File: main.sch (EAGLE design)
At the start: 27 parts, among them IC1 FT232RL, U1 ATMEGA328P_TQFP, Y3 16MHz

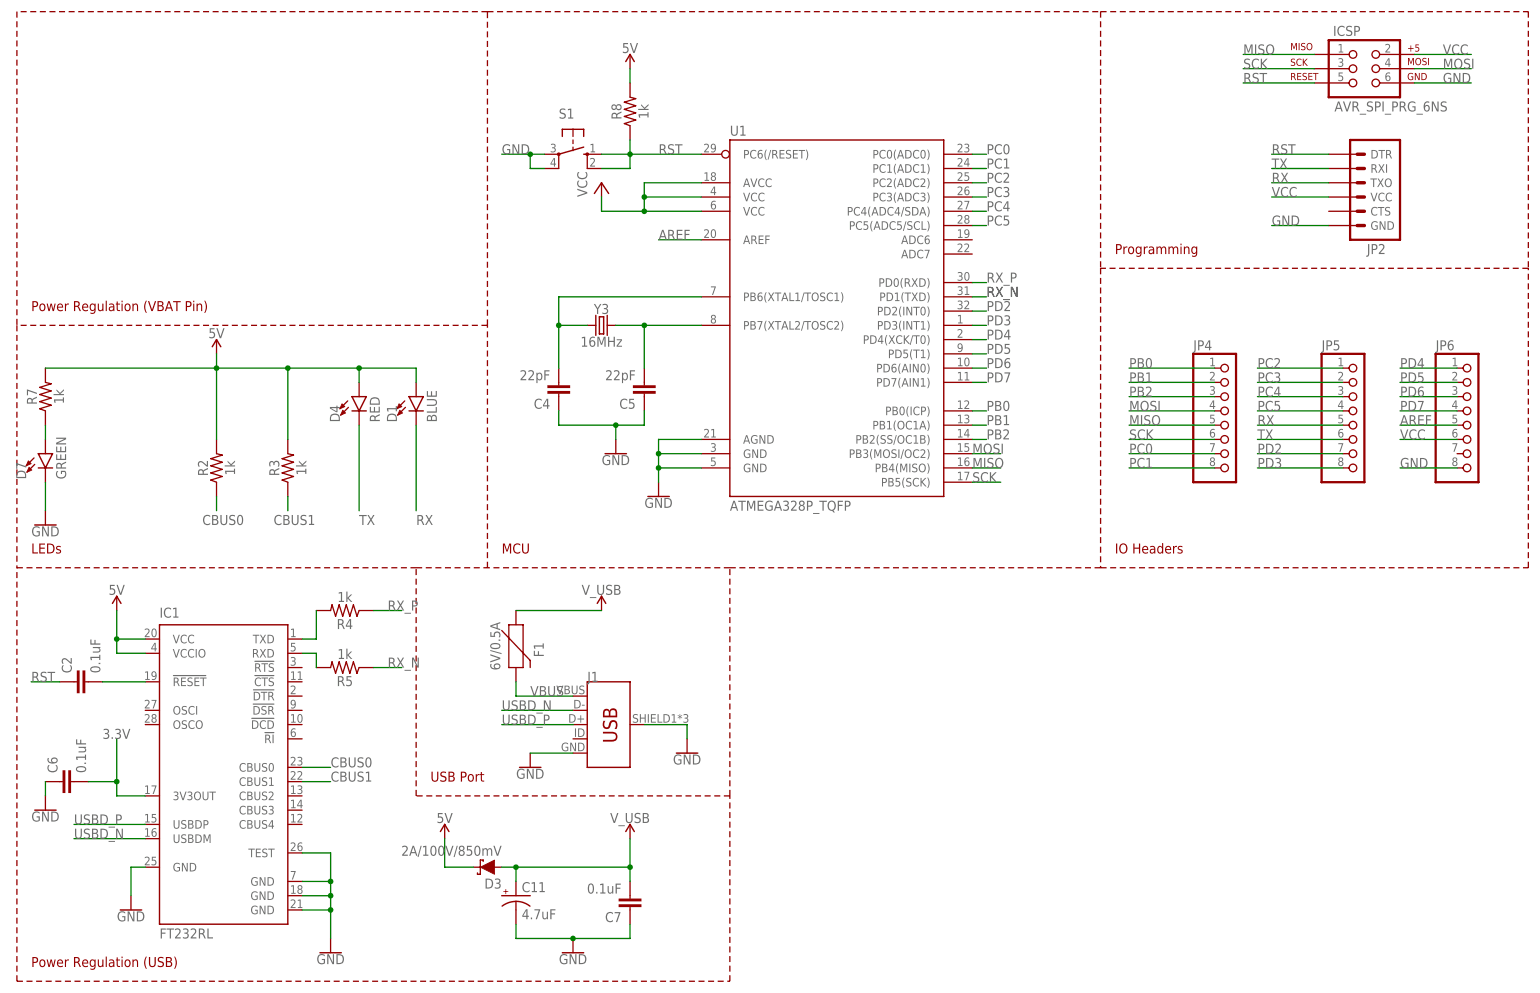
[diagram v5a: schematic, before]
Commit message: Fixed DRC Errors
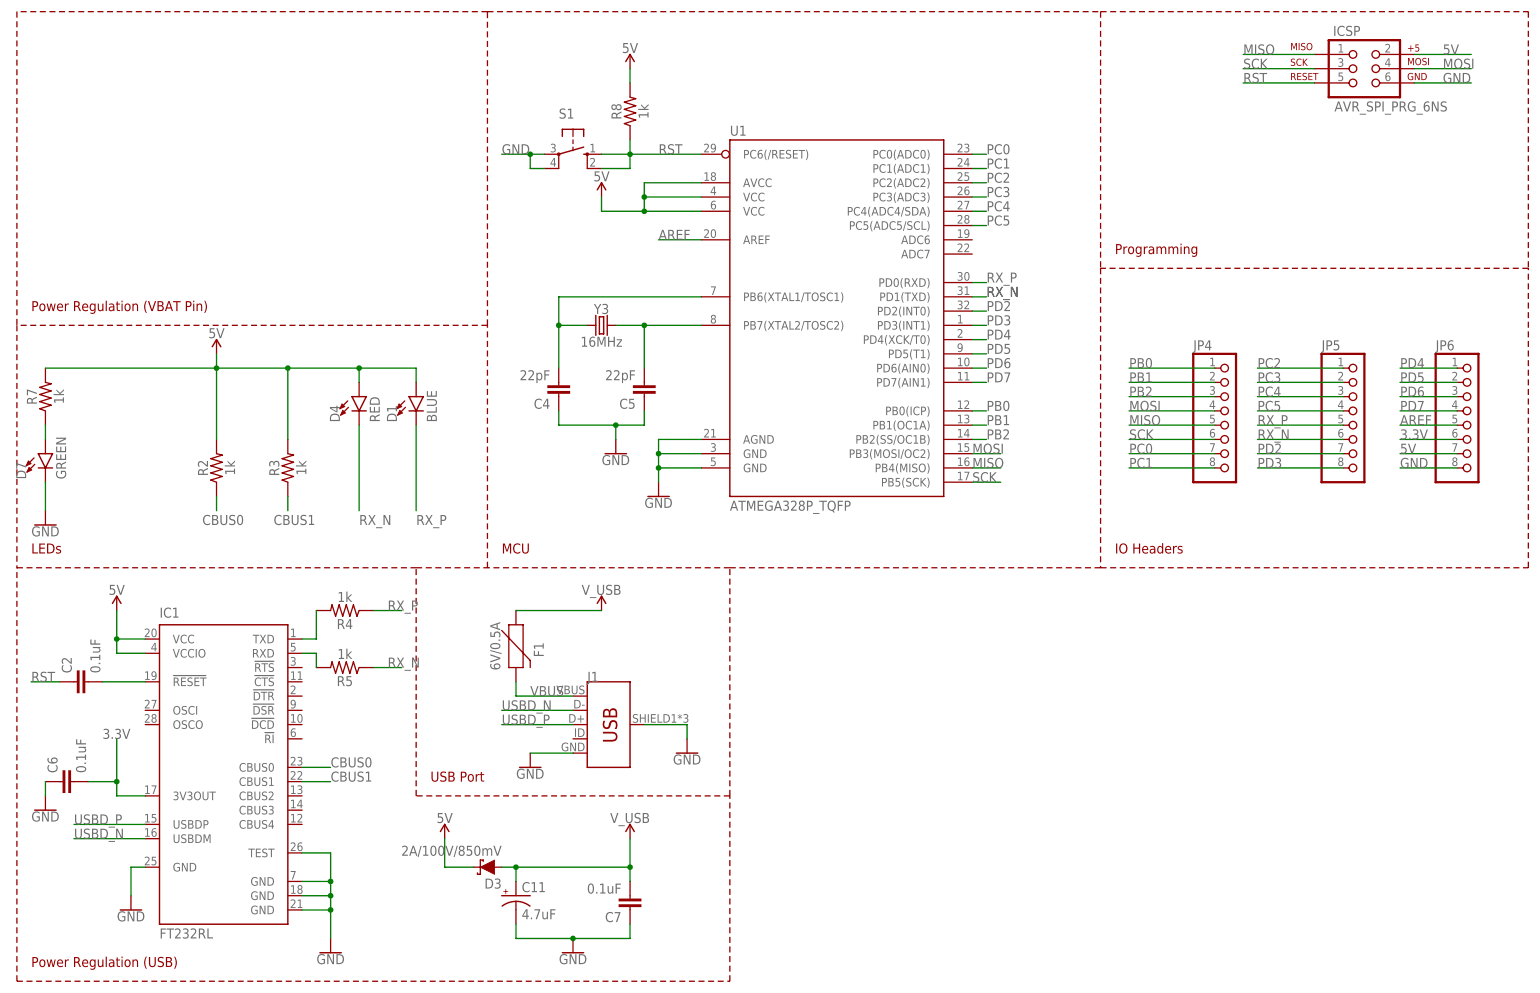
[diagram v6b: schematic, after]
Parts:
- removed JP2: (no value), SparkFun-Connectors:ARDUINO_SERIAL_PROGRAMLOCK
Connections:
- removed net RX: D1.C, JP2.TXO, JP5.5
- removed net TX: D4.C, JP2.RXI, JP5.6
- removed net VCC: ICSP.2, JP2.VCC, JP6.6, U1.AVCC, U1.VCC@4, U1.VCC@6
- net 3.3V: now also JP6.6
- net 5V: now also ICSP.2, JP6.7, U1.AVCC, U1.VCC@4, U1.VCC@6
- net GND: no longer JP2.GND
- net RST: no longer JP2.DTR
- net RX_N: now also D4.C, JP5.6
- net RX_P: now also D1.C, JP5.5
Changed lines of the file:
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@@
 <parts>
 <part name="ICSP" library="SparkFun-Connectors" deviceset="AVR_SPI_PRG_6" device="NS"/>
-<part name="JP2" library="SparkFun-Connectors" deviceset="ARDUINO_SERIAL_PROGRAM" device="LOCK"/>
 <part name="JP4" library="pinhead" library_urn="urn:adsk.eagle:library:325" deviceset="PINHD-1X8" device=""/>
 <part name="JP5" library="pinhead" library_urn="urn:adsk.eagle:library:325" deviceset="PINHD-1X8" device=""/>
@@
 <part name="D1" library="SparkFun-LED" deviceset="LED-BLUE" device="0603" value="BLUE"/>
 <part name="IC1" library="ftdichip" library_urn="urn:adsk.eagle:library:231" deviceset="FT232R" device="L"/>
-<part name="P+4" library="supply1" library_urn="urn:adsk.eagle:library:371" deviceset="VCC" device=""/>
 <part name="J1" library="SparkFun-Connectors" deviceset="USB_MICRO-B" device="_FEMALE-SMT"/>
 <part name="F1" library="SparkFun-Fuses" deviceset="PPTC" device="_HALF-AMP" value="6V/0.5A"/>
@@
 <part name="D7" library="SparkFun-LED" deviceset="LED-GREEN" device="0603" value="GREEN"/>
 <part name="D4" library="SparkFun-LED" deviceset="LED-RED" device="0603" value="RED"/>
+<part name="SUPPLY3" library="SparkFun-PowerSymbols" deviceset="5V" device=""/>
 </parts>
 <sheets>
@@
 <instances>
 <instance part="ICSP" gate="G$1" x="198.12" y="144.78"/>
-<instance part="JP2" gate="G$1" x="198.12" y="124.46" rot="R180"/>
 <instance part="JP4" gate="A" x="175.26" y="81.28"/>
 <instance part="JP5" gate="A" x="198.12" y="81.28"/>
@@
 <instance part="D1" gate="G$1" x="30.48" y="86.36"/>
 <instance part="IC1" gate="1" x="-5.08" y="20.32"/>
-<instance part="P+4" gate="VCC" x="63.5" y="124.46"/>
 <instance part="J1" gate="G$1" x="63.5" y="27.94"/>
 <instance part="F1" gate="G$1" x="48.26" y="43.18" rot="R270"/>
@@
 <instance part="D7" gate="G$1" x="-35.56" y="76.2"/>
 <instance part="D4" gate="G$1" x="20.32" y="86.36"/>
+<instance part="SUPPLY3" gate="G$1" x="63.5" y="121.92"/>
 </instances>
 <busses>
@@
 <wire x1="208.28" y1="142.24" x2="218.44" y2="142.24" width="0.1524" layer="91"/>
 <label x="213.36" y="142.24" size="1.778" layer="95"/>
-</segment>
-<segment>
-<pinref part="JP2" gate="G$1" pin="GND"/>
-<wire x1="193.04" y1="116.84" x2="182.88" y2="116.84" width="0.1524" layer="91"/>
-<label x="182.88" y="116.84" size="1.778" layer="95"/>
 </segment>
 <segment>
@@
 </segment>
 </net>
-<net name="VCC" class="3">
-<segment>
-<pinref part="ICSP" gate="G$1" pin="2"/>
-<wire x1="208.28" y1="147.32" x2="218.44" y2="147.32" width="0.1524" layer="91"/>
-<label x="213.36" y="147.32" size="1.778" layer="95"/>
-</segment>
-<segment>
-<pinref part="JP2" gate="G$1" pin="VCC"/>
-<wire x1="193.04" y1="121.92" x2="182.88" y2="121.92" width="0.1524" layer="91"/>
-<label x="182.88" y="121.92" size="1.778" layer="95"/>
-</segment>
-<segment>
-<pinref part="JP6" gate="A" pin="6"/>
-<wire x1="215.9" y1="78.74" x2="205.74" y2="78.74" width="0.1524" layer="91"/>
-<label x="205.74" y="78.74" size="1.778" layer="95"/>
-</segment>
-<segment>
-<wire x1="81.28" y1="121.92" x2="71.12" y2="121.92" width="0.1524" layer="91"/>
-<wire x1="81.28" y1="124.46" x2="71.12" y2="124.46" width="0.1524" layer="91"/>
-<wire x1="81.28" y1="119.38" x2="71.12" y2="119.38" width="0.1524" layer="91"/>
-<wire x1="71.12" y1="119.38" x2="71.12" y2="121.92" width="0.1524" layer="91"/>
-<wire x1="71.12" y1="121.92" x2="71.12" y2="124.46" width="0.1524" layer="91"/>
-<junction x="71.12" y="121.92"/>
-<wire x1="71.12" y1="119.38" x2="63.5" y2="119.38" width="0.1524" layer="91"/>
-<junction x="71.12" y="119.38"/>
-<pinref part="P+4" gate="VCC" pin="VCC"/>
-<wire x1="63.5" y1="119.38" x2="63.5" y2="121.92" width="0.1524" layer="91"/>
-<pinref part="U1" gate="U$1" pin="VCC@4"/>
-<pinref part="U1" gate="U$1" pin="VCC@6"/>
-<pinref part="U1" gate="U$1" pin="AVCC"/>
-</segment>
-</net>
 <net name="RST" class="0">
 <segment>
@@
 </segment>
 <segment>
-<wire x1="193.04" y1="129.54" x2="182.88" y2="129.54" width="0.1524" layer="91"/>
-<label x="182.88" y="129.54" size="1.778" layer="95"/>
-<pinref part="JP2" gate="G$1" pin="DTR"/>
-</segment>
-<segment>
 <wire x1="-33.02" y1="35.56" x2="-38.1" y2="35.56" width="0.1524" layer="91"/>
 <label x="-38.1" y="35.56" size="1.778" layer="95"/>
@@
 <wire x1="172.72" y1="83.82" x2="157.48" y2="83.82" width="0.1524" layer="91"/>
 <label x="157.48" y="83.82" size="1.778" layer="95"/>
-</segment>
-</net>
-<net name="TX" class="0">
-<segment>
-<pinref part="JP2" gate="G$1" pin="RXI"/>
-<wire x1="193.04" y1="127" x2="182.88" y2="127" width="0.1524" layer="91"/>
-<label x="182.88" y="127" size="1.778" layer="95"/>
-</segment>
-<segment>
-<pinref part="JP5" gate="A" pin="6"/>
-<wire x1="195.58" y1="78.74" x2="180.34" y2="78.74" width="0.1524" layer="91"/>
-<label x="180.34" y="78.74" size="1.778" layer="95"/>
-</segment>
-<segment>
-<label x="20.32" y="63.5" size="1.778" layer="95"/>
-<pinref part="D4" gate="G$1" pin="C"/>
-<wire x1="20.32" y1="66.04" x2="20.32" y2="81.28" width="0.1524" layer="91"/>
-</segment>
-</net>
-<net name="RX" class="0">
-<segment>
-<pinref part="JP2" gate="G$1" pin="TXO"/>
-<wire x1="193.04" y1="124.46" x2="182.88" y2="124.46" width="0.1524" layer="91"/>
-<label x="182.88" y="124.46" size="1.778" layer="95"/>
-</segment>
-<segment>
-<pinref part="JP5" gate="A" pin="5"/>
-<wire x1="195.58" y1="81.28" x2="180.34" y2="81.28" width="0.1524" layer="91"/>
-<label x="180.34" y="81.28" size="1.778" layer="95"/>
-</segment>
-<segment>
-<label x="30.48" y="63.5" size="1.778" layer="95"/>
-<pinref part="D1" gate="G$1" pin="C"/>
-<wire x1="30.48" y1="66.04" x2="30.48" y2="81.28" width="0.1524" layer="91"/>
 </segment>
 </net>
@@
 <pinref part="SUPPLY8" gate="G$1" pin="5V"/>
 </segment>
+<segment>
+<pinref part="ICSP" gate="G$1" pin="2"/>
+<wire x1="208.28" y1="147.32" x2="218.44" y2="147.32" width="0.1524" layer="91"/>
+<label x="213.36" y="147.32" size="1.778" layer="95"/>
+</segment>
+<segment>
+<wire x1="81.28" y1="121.92" x2="71.12" y2="121.92" width="0.1524" layer="91"/>
+<wire x1="81.28" y1="124.46" x2="71.12" y2="124.46" width="0.1524" layer="91"/>
+<wire x1="81.28" y1="119.38" x2="71.12" y2="119.38" width="0.1524" layer="91"/>
+<wire x1="71.12" y1="119.38" x2="71.12" y2="121.92" width="0.1524" layer="91"/>
+<wire x1="71.12" y1="121.92" x2="71.12" y2="124.46" width="0.1524" layer="91"/>
+<junction x="71.12" y="121.92"/>
+<wire x1="71.12" y1="119.38" x2="63.5" y2="119.38" width="0.1524" layer="91"/>
+<junction x="71.12" y="119.38"/>
+<pinref part="U1" gate="U$1" pin="VCC@4"/>
+<pinref part="U1" gate="U$1" pin="VCC@6"/>
+<pinref part="U1" gate="U$1" pin="AVCC"/>
+<pinref part="SUPPLY3" gate="G$1" pin="5V"/>
+<wire x1="63.5" y1="119.38" x2="63.5" y2="121.92" width="0.1524" layer="91"/>
+</segment>
+<segment>
+<wire x1="215.9" y1="76.2" x2="205.74" y2="76.2" width="0.1524" layer="91"/>
+<label x="205.74" y="76.2" size="1.778" layer="95"/>
+<pinref part="JP6" gate="A" pin="7"/>
+</segment>
 </net>
 <net name="3.3V" class="0">
@@
 <label x="-25.4" y="25.4" size="1.778" layer="95"/>
 </segment>
+<segment>
+<pinref part="JP6" gate="A" pin="6"/>
+<wire x1="215.9" y1="78.74" x2="205.74" y2="78.74" width="0.1524" layer="91"/>
+<label x="205.74" y="78.74" size="1.778" layer="95"/>
+</segment>
 </net>
 <net name="USBD_P" class="0">
@@
 <pinref part="U1" gate="U$1" pin="PD0(RXD)"/>
 </segment>
+<segment>
+<label x="30.48" y="63.5" size="1.778" layer="95"/>
+<pinref part="D1" gate="G$1" pin="C"/>
+<wire x1="30.48" y1="66.04" x2="30.48" y2="81.28" width="0.1524" layer="91"/>
+</segment>
+<segment>
+<pinref part="JP5" gate="A" pin="5"/>
+<wire x1="195.58" y1="81.28" x2="180.34" y2="81.28" width="0.1524" layer="91"/>
+<label x="180.34" y="81.28" size="1.778" layer="95"/>
+</segment>
 </net>
 <net name="RX_N" class="0">
@@
 <pinref part="U1" gate="U$1" pin="PD1(TXD)"/>
 </segment>
-</net>
+<segment>
+<label x="20.32" y="63.5" size="1.778" layer="95"/>
+<pinref part="D4" gate="G$1" pin="C"/>
+<wire x1="20.32" y1="66.04" x2="20.32" y2="81.28" width="0.1524" layer="91"/>
+</segment>
+<segment>
+<pinref part="JP5" gate="A" pin="6"/>
+<wire x1="195.58" y1="78.74" x2="180.34" y2="78.74" width="0.1524" layer="91"/>
+<label x="180.34" y="78.74" size="1.778" layer="95"/>
+</segment>
+</net>

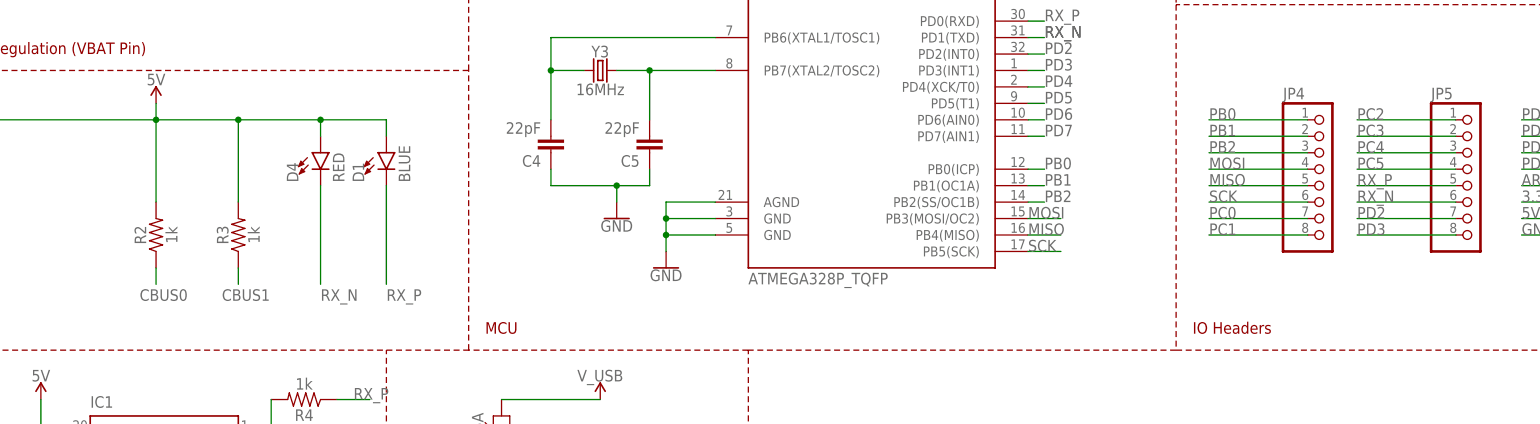
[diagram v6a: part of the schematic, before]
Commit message: Changes LED drivers to CBUS0 and CBUS1
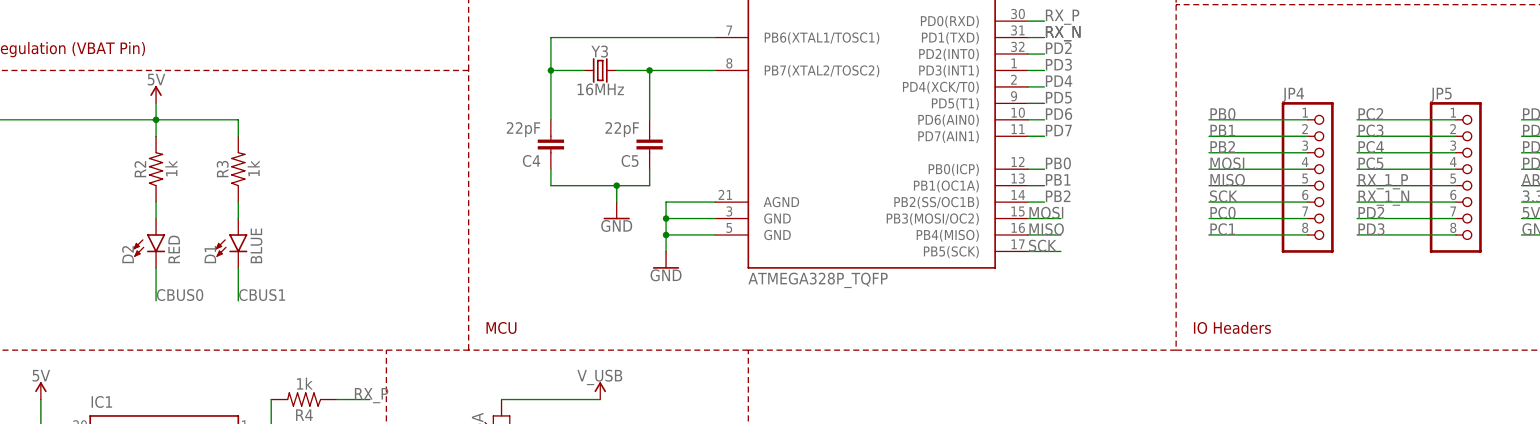
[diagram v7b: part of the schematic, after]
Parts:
- removed D4: RED, SparkFun-LED:LED-RED0603
- added D2: RED, SparkFun-LED:LED-RED0603
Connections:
- new net N$1: D1.A, R3.1
- new net N$2: D2.A, R2.1
- net 5V: no longer D1.A, D4.A
- net CBUS0: now also D2.C; no longer R2.1
- net CBUS1: now also D1.C; no longer R3.1
- net RX_1_N: now also JP5.6
- net RX_1_P: now also JP5.5
- net RX_N: no longer D4.C, JP5.6
- net RX_P: no longer D1.C, JP5.5
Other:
- moved on the sheet: D1, R2, R3
